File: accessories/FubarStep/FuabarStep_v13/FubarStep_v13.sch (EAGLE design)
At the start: 80 parts, among them IC2 SN754410NE, IC3 SN754410NE, U1 FUBARINO_SD, U2 FUBARINO_MINI, U3 OKI-78SR-5/1.5-W36H-C, X1 DC21MMX

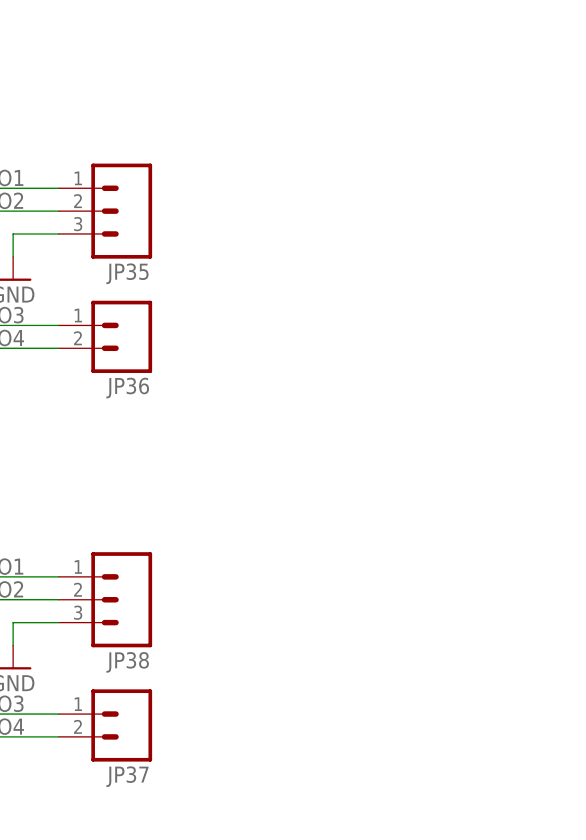
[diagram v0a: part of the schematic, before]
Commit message: Version 1.3 ready for review. Added pull down resistors to H-Bridge inputs, tweaked part placement for better assembly and silk screen for more information and readability.
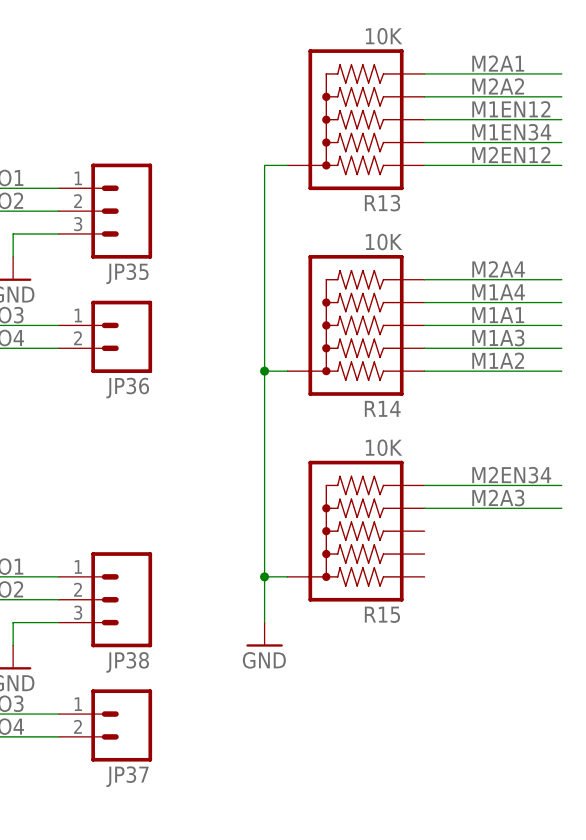
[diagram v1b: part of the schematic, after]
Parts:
- added R13, R14, R15: 10K, SparkFun-Resistors:RPACK-BUSSED-SIP-PTH-5
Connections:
- net GND: now also R13.1, R14.1, R15.1
- net M1A1: now also R14.4
- net M1A2: now also R14.2
- net M1A3: now also R14.3
- net M1A4: now also R14.5
- net M1EN12: now also R13.4
- net M1EN34: now also R13.3
- net M2A1: now also R13.6
- net M2A2: now also R13.5
- net M2A3: now also R15.5
- net M2A4: now also R14.6
- net M2EN12: now also R13.2
- net M2EN34: now also R15.6
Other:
- note added: "FUBARStep v1.3"
- note added: "Pull Downs"
- note added: "v1.3 : 02/01/2014 Added pull down resistors Separated servo headers Moved all motor screw terminals together Moved PWRSEL jumper Silk thickness changed Fixed lower left mounting hole location FB Mini now on .1 grid"
- note removed: "FUBARStep v1.2"
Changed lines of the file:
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@@
 <part name="C4" library="SchmalzHaus" deviceset="CAP_ELECTROLYTIC" device="PTH1_BPS" value="100uF"/>
 <part name="C6" library="SchmalzHaus" deviceset="CAP_ELECTROLYTIC" device="PTH1_BPS" value="100uF"/>
+<part name="GND35" library="supply1" deviceset="GND" device=""/>
+<part name="R13" library="SparkFun-Resistors" deviceset="RPACK" device="-BUSSED-SIP-PTH-5" value="10K"/>
+<part name="R14" library="SparkFun-Resistors" deviceset="RPACK" device="-BUSSED-SIP-PTH-5" value="10K"/>
+<part name="R15" library="SparkFun-Resistors" deviceset="RPACK" device="-BUSSED-SIP-PTH-5" value="10K"/>
 </parts>
 <sheets>
 <sheet>
 <plain>
-<text x="12.7" y="246.38" size="6.4516" layer="98">FUBARStep v1.2</text>
+<text x="12.7" y="246.38" size="6.4516" layer="98">FUBARStep v1.3</text>
 <text x="7.62" y="152.4" size="1.778" layer="98">FTDI Serial</text>
 <text x="99.06" y="170.18" size="1.778" layer="98">RC Servo/5V tolerant GPIO</text>
@@
   Changed 100uF cap footprint slightly
   Moved things around for easier assembly</text>
+<wire x1="335.28" y1="248.92" x2="381" y2="248.92" width="0.1524" layer="98"/>
+<wire x1="381" y1="248.92" x2="381" y2="139.7" width="0.1524" layer="98"/>
+<wire x1="381" y1="139.7" x2="335.28" y2="139.7" width="0.1524" layer="98"/>
+<text x="337.82" y="246.38" size="1.778" layer="98">Pull Downs</text>
+<text x="266.7" y="86.36" size="1.778" layer="98">v1.3 : 02/01/2014
+  Added pull down resistors
+  Separated servo headers
+  Moved all motor screw terminals together
+  Moved PWRSEL jumper
+  Silk thickness changed
+  Fixed lower left mounting hole location
+  FB Mini now on .1 grid</text>
 </plain>
 <instances>
@@
 <instance part="C4" gate="G$1" x="185.42" y="220.98"/>
 <instance part="C6" gate="G$1" x="185.42" y="160.02"/>
+<instance part="GND35" gate="1" x="340.36" y="175.26"/>
+<instance part="R13" gate="G$1" x="358.14" y="228.6" rot="R180"/>
+<instance part="R14" gate="G$1" x="358.14" y="205.74" rot="R180"/>
+<instance part="R15" gate="G$1" x="358.14" y="182.88" rot="R180"/>
 </instances>
 <busses>
@@
 <junction x="254" y="106.68"/>
 </segment>
+<segment>
+<pinref part="GND35" gate="1" pin="GND"/>
+<wire x1="340.36" y1="228.6" x2="340.36" y2="205.74" width="0.1524" layer="91"/>
+<pinref part="R13" gate="G$1" pin="1"/>
+<wire x1="340.36" y1="205.74" x2="340.36" y2="182.88" width="0.1524" layer="91"/>
+<wire x1="340.36" y1="182.88" x2="340.36" y2="177.8" width="0.1524" layer="91"/>
+<wire x1="340.36" y1="228.6" x2="342.9" y2="228.6" width="0.1524" layer="91"/>
+<pinref part="R14" gate="G$1" pin="1"/>
+<wire x1="340.36" y1="205.74" x2="342.9" y2="205.74" width="0.1524" layer="91"/>
+<junction x="340.36" y="205.74"/>
+<pinref part="R15" gate="G$1" pin="1"/>
+<wire x1="340.36" y1="182.88" x2="342.9" y2="182.88" width="0.1524" layer="91"/>
+<junction x="340.36" y="182.88"/>
+</segment>
 </net>
 <net name="VIN" class="0">
@@
 <label x="99.06" y="94.488" size="1.778" layer="95"/>
 </segment>
+<segment>
+<wire x1="358.14" y1="238.76" x2="373.38" y2="238.76" width="0.1524" layer="91"/>
+<label x="363.22" y="239.014" size="1.778" layer="95"/>
+<pinref part="R13" gate="G$1" pin="6"/>
+</segment>
 </net>
 <net name="M2A4" class="0">
@@
 <label x="99.06" y="107.188" size="1.778" layer="95"/>
 </segment>
+<segment>
+<wire x1="358.14" y1="215.9" x2="373.38" y2="215.9" width="0.1524" layer="91"/>
+<label x="363.22" y="216.154" size="1.778" layer="95"/>
+<pinref part="R14" gate="G$1" pin="6"/>
+</segment>
 </net>
 <net name="M2A3" class="0">
@@
 <label x="121.92" y="145.034" size="1.778" layer="95"/>
 </segment>
+<segment>
+<wire x1="358.14" y1="190.5" x2="373.38" y2="190.5" width="0.1524" layer="91"/>
+<label x="363.22" y="190.754" size="1.778" layer="95"/>
+<pinref part="R15" gate="G$1" pin="5"/>
+</segment>
 </net>
 <net name="M2A2" class="0">
@@
 <label x="99.06" y="81.788" size="1.778" layer="95"/>
 </segment>
+<segment>
+<wire x1="358.14" y1="236.22" x2="373.38" y2="236.22" width="0.1524" layer="91"/>
+<label x="363.22" y="236.474" size="1.778" layer="95"/>
+<pinref part="R13" gate="G$1" pin="5"/>
+</segment>
 </net>
 <net name="M1A2" class="0">
@@
 <label x="99.06" y="157.988" size="1.778" layer="95"/>
 </segment>
+<segment>
+<wire x1="358.14" y1="205.74" x2="373.38" y2="205.74" width="0.1524" layer="91"/>
+<label x="363.22" y="205.994" size="1.778" layer="95"/>
+<pinref part="R14" gate="G$1" pin="2"/>
+</segment>
 </net>
 <net name="M1A3" class="0">
@@
 <label x="99.06" y="145.288" size="1.778" layer="95"/>
 </segment>
+<segment>
+<wire x1="358.14" y1="208.28" x2="373.38" y2="208.28" width="0.1524" layer="91"/>
+<label x="363.22" y="208.534" size="1.778" layer="95"/>
+<pinref part="R14" gate="G$1" pin="3"/>
+</segment>
 </net>
 <net name="M1A4" class="0">
@@
 <label x="99.06" y="119.888" size="1.778" layer="95"/>
 </segment>
+<segment>
+<wire x1="358.14" y1="213.36" x2="373.38" y2="213.36" width="0.1524" layer="91"/>
+<label x="363.22" y="213.614" size="1.778" layer="95"/>
+<pinref part="R14" gate="G$1" pin="5"/>
+</segment>
 </net>
 <net name="M1A1" class="0">
@@
 <label x="99.06" y="132.588" size="1.778" layer="95"/>
 </segment>
+<segment>
+<wire x1="358.14" y1="210.82" x2="373.38" y2="210.82" width="0.1524" layer="91"/>
+<label x="363.22" y="211.074" size="1.778" layer="95"/>
+<pinref part="R14" gate="G$1" pin="4"/>
+</segment>
 </net>
 <net name="M1EN34" class="0">
@@
 <label x="99.06" y="56.388" size="1.778" layer="95"/>
 </segment>
+<segment>
+<wire x1="358.14" y1="231.14" x2="373.38" y2="231.14" width="0.1524" layer="91"/>
+<label x="363.22" y="231.394" size="1.778" layer="95"/>
+<pinref part="R13" gate="G$1" pin="3"/>
+</segment>
 </net>
 <net name="M1EN12" class="0">
@@
 <label x="99.06" y="69.088" size="1.778" layer="95"/>
 </segment>
+<segment>
+<wire x1="358.14" y1="233.68" x2="373.38" y2="233.68" width="0.1524" layer="91"/>
+<label x="363.22" y="233.934" size="1.778" layer="95"/>
+<pinref part="R13" gate="G$1" pin="4"/>
+</segment>
 </net>
 <net name="M2EN34" class="0">
@@
 <label x="121.92" y="157.734" size="1.778" layer="95"/>
 </segment>
+<segment>
+<wire x1="358.14" y1="193.04" x2="373.38" y2="193.04" width="0.1524" layer="91"/>
+<label x="363.22" y="193.294" size="1.778" layer="95"/>
+<pinref part="R15" gate="G$1" pin="6"/>
+</segment>
 </net>
 <net name="M2EN12" class="0">
@@
 <label x="99.06" y="43.688" size="1.778" layer="95"/>
 </segment>
-</net>
+<segment>
+<wire x1="358.14" y1="228.6" x2="373.38" y2="228.6" width="0.1524" layer="91"/>
+<label x="363.22" y="228.854" size="1.778" layer="95"/>
+<pinref part="R13" gate="G$1" pin="2"/>
+</segment>
+</net>
